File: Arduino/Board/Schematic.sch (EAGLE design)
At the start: 43 parts, among them Q1 2N7002E, Q2 2N7002E, Q3 2N7002E

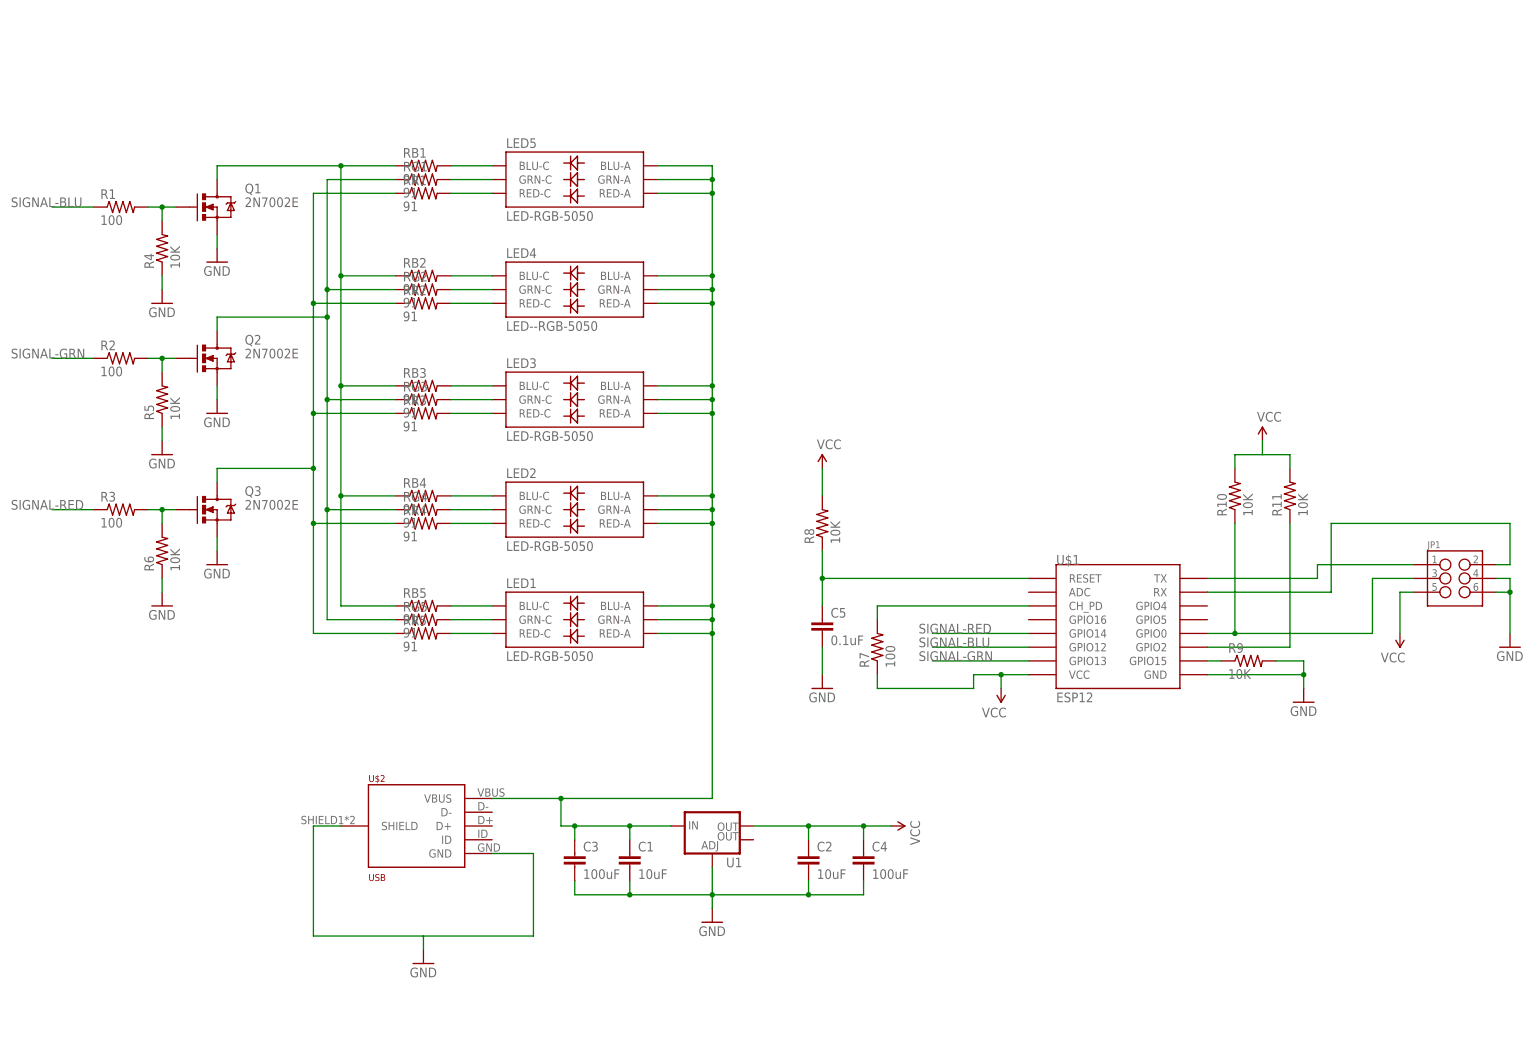
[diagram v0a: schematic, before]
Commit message: pcb upgrade
changed:
- bigger (size) resistors for LEDs
- changed MOSFETs for more power
- added ambient light sensors
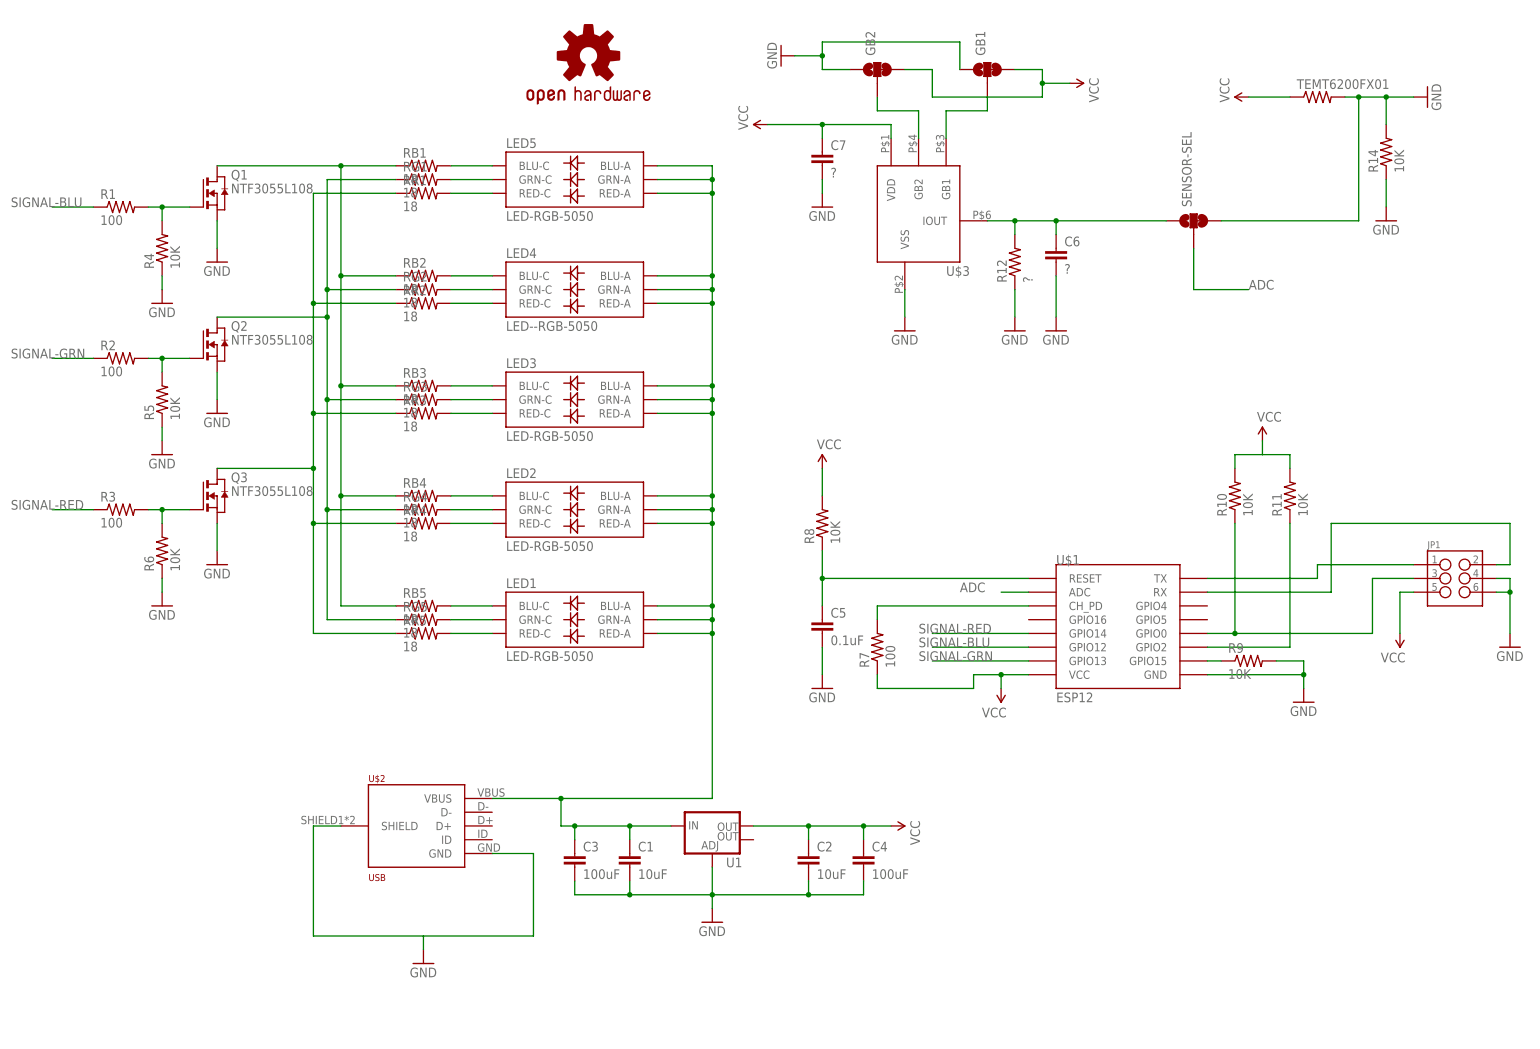
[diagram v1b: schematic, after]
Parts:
- added C6, C7: ?, SparkFun-Capacitors:CAP0603-CAP
- added GB1, GB2, SENSOR-SEL: JUMPER-PAD-3-2OF3_NC_BY_TRACE_LARGE, SparkFun-Passives:JUMPER-PAD-3-2OF3_NC_BY_TRACE_LARGE
- added LOGO1: OSHW-LOGOM-COPPER, SparkFun-Aesthetics:OSHW-LOGOM-COPPER
- added R12: ?, SparkFun-Passives:RESISTOR0805-RES
- added R14: 10K, SparkFun-Passives:RESISTOR0805-RES
- added TEMT6200FX01: (no value), SparkFun-Passives:RESISTOR0805-RES
- added U$3: NOA1212, MCustom:NOA1212
- Q1, Q2, Q3: value 2N7002E -> NTF3055L108; device SparkFun-DiscreteSemi:MOSFET-NCHANNELAO3404A -> zetex:NMOSSOT223
- RB1, RB2, RB3, RB4, RB5, RG1, RG2, RG3, RG4, RG5, RR1, RR2, RR3, RR4, RR5: value 91 -> 18; device SparkFun-Passives:RESISTOR0805-RES -> SparkFun-Passives:RESISTOR1206
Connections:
- new net ADC: SENSOR-SEL.2, U$1.ADC
- new net N$1111: C6.1, R12.2, SENSOR-SEL.1, U$3.IOUT
- new net N$51: GB2.2, U$3.GB2
- new net N$54: GB1.2, U$3.GB1
- net GND: now also C6.2, C7.2, GB1.1, GB2.1, R12.1, R14.1, R14.2, SENSOR-SEL.3, TEMT6200FX01.2, U$3.VSS
- net VCC: now also C7.1, GB1.3, GB2.3, TEMT6200FX01.1, U$3.VDD

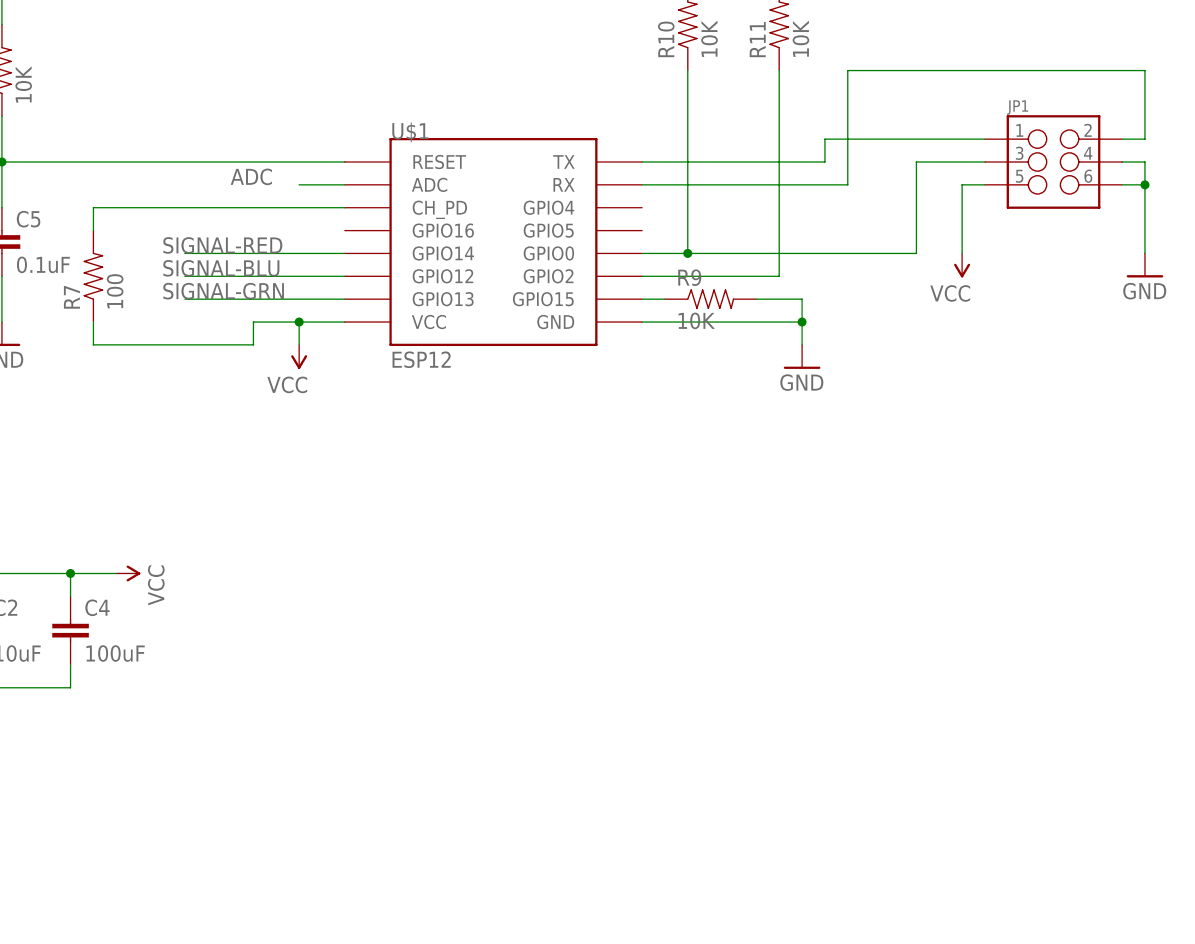
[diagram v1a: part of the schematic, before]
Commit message: added buzzer
added buzzer and holes for air flow
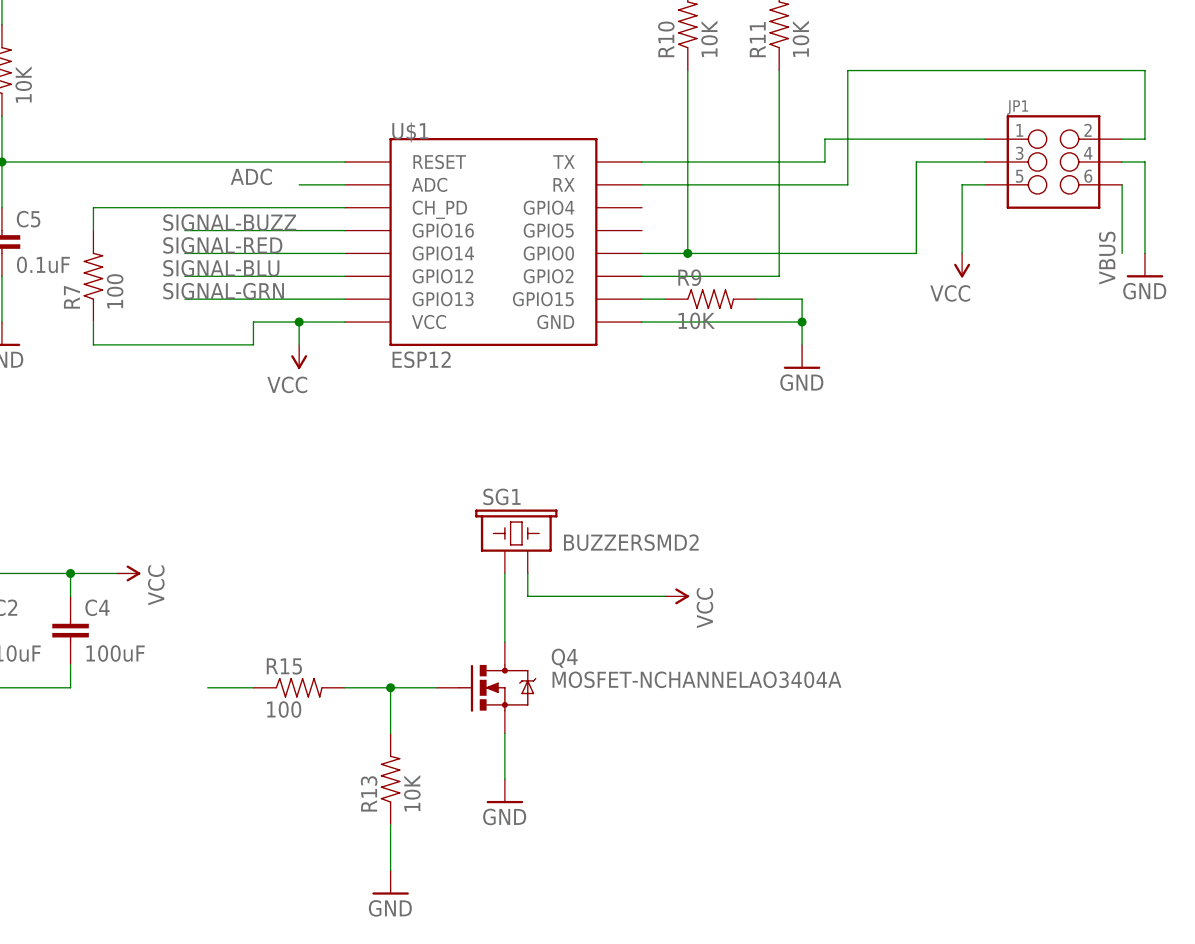
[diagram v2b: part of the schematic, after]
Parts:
- added Q4: MOSFET-NCHANNELAO3404A, SparkFun-DiscreteSemi:MOSFET-NCHANNELAO3404A
- added R13: 10K, SparkFun-Passives:RESISTOR0805-RES
- added R15: 100, SparkFun-Passives:RESISTOR0805-RES
- added SG1: BUZZERSMD2, SparkFun-Electromechanical:BUZZERSMD2
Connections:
- removed net N$2: C1.1, C3.1, LED1.BLU-A, LED1.GRN-A, LED1.RED-A, LED2.BLU-A, LED2.GRN-A, LED2.RED-A, LED3.BLU-A, LED3.GRN-A, LED3.RED-A, LED4.BLU-A, LED4.GRN-A, LED4.RED-A, LED5.BLU-A, LED5.GRN-A, LED5.RED-A, U$2.VBUS, U1.IN
- new net N$82: Q4.G, R13.2, R15.2
- new net N$83: Q4.D, SG1.1
- new net SIGNAL-BUZZ: R15.1, U$1.GPIO16
- new net VBUS: C1.1, C3.1, JP1.6, LED1.BLU-A, LED1.GRN-A, LED1.RED-A, LED2.BLU-A, LED2.GRN-A, LED2.RED-A, LED3.BLU-A, LED3.GRN-A, LED3.RED-A, LED4.BLU-A, LED4.GRN-A, LED4.RED-A, LED5.BLU-A, LED5.GRN-A, LED5.RED-A, U$2.VBUS, U1.IN
- net GND: now also Q4.S, R13.1; no longer JP1.6
- net VCC: now also SG1.2

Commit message: updated the board design
updated to the requirements in the https://trello.com/c/WxGEJiPR
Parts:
- added R16, R17: 10K, SparkFun-Passives:RESISTOR0805-RES
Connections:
- net GND: now also R16.2, R17.2
- net N$52: now also R17.1
- net N$53: now also R16.1
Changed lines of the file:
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@@
 <part name="GND19" library="SparkFun-Aesthetics" deviceset="GND" device=""/>
 <part name="GND20" library="SparkFun-Aesthetics" deviceset="GND" device=""/>
+<part name="R16" library="SparkFun-Passives" deviceset="RESISTOR" device="0805-RES" value="10K"/>
+<part name="R17" library="SparkFun-Passives" deviceset="RESISTOR" device="0805-RES" value="10K"/>
+<part name="GND21" library="SparkFun-Aesthetics" deviceset="GND" device=""/>
 </parts>
 <sheets>
@@
 <instance part="GND19" gate="1" x="124.46" y="12.7"/>
 <instance part="GND20" gate="1" x="137.16" y="22.86"/>
+<instance part="R16" gate="G$1" x="177.8" y="116.84" rot="R90"/>
+<instance part="R17" gate="G$1" x="187.96" y="116.84" rot="R90"/>
+<instance part="GND21" gate="1" x="182.88" y="137.16" rot="R180"/>
 </instances>
 <busses>
@@
 <wire x1="137.16" y1="30.48" x2="137.16" y2="25.4" width="0.1524" layer="91"/>
 <pinref part="GND20" gate="1" pin="GND"/>
+</segment>
+<segment>
+<pinref part="R16" gate="G$1" pin="2"/>
+<wire x1="177.8" y1="121.92" x2="177.8" y2="127" width="0.1524" layer="91"/>
+<wire x1="177.8" y1="127" x2="182.88" y2="127" width="0.1524" layer="91"/>
+<pinref part="R17" gate="G$1" pin="2"/>
+<wire x1="182.88" y1="127" x2="187.96" y2="127" width="0.1524" layer="91"/>
+<wire x1="187.96" y1="127" x2="187.96" y2="121.92" width="0.1524" layer="91"/>
+<pinref part="GND21" gate="1" pin="GND"/>
+<wire x1="182.88" y1="127" x2="182.88" y2="134.62" width="0.1524" layer="91"/>
 </segment>
 </net>
@@
 <wire x1="172.72" y1="93.98" x2="172.72" y2="96.52" width="0.1524" layer="91"/>
 <pinref part="JP1" gate="G$1" pin="1"/>
-<wire x1="172.72" y1="96.52" x2="190.5" y2="96.52" width="0.1524" layer="91"/>
+<wire x1="172.72" y1="96.52" x2="187.96" y2="96.52" width="0.1524" layer="91"/>
+<pinref part="R17" gate="G$1" pin="1"/>
+<wire x1="187.96" y1="96.52" x2="190.5" y2="96.52" width="0.1524" layer="91"/>
+<wire x1="187.96" y1="96.52" x2="187.96" y2="111.76" width="0.1524" layer="91"/>
+<junction x="187.96" y="96.52"/>
 </segment>
 </net>
@@
 <wire x1="152.4" y1="91.44" x2="175.26" y2="91.44" width="0.1524" layer="91"/>
 <wire x1="175.26" y1="91.44" x2="175.26" y2="104.14" width="0.1524" layer="91"/>
-<wire x1="175.26" y1="104.14" x2="208.28" y2="104.14" width="0.1524" layer="91"/>
+<wire x1="175.26" y1="104.14" x2="177.8" y2="104.14" width="0.1524" layer="91"/>
+<wire x1="177.8" y1="104.14" x2="208.28" y2="104.14" width="0.1524" layer="91"/>
 <wire x1="208.28" y1="104.14" x2="208.28" y2="96.52" width="0.1524" layer="91"/>
 <pinref part="JP1" gate="G$1" pin="2"/>
 <wire x1="208.28" y1="96.52" x2="205.74" y2="96.52" width="0.1524" layer="91"/>
-</segment>
-</net>
+<pinref part="R16" gate="G$1" pin="1"/>
+<wire x1="177.8" y1="104.14" x2="177.8" y2="111.76" width="0.1524" layer="91"/>
+<junction x="177.8" y="104.14"/>
+</segment>
+</net>
